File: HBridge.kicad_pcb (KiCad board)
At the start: 2 copper layers, 28 parts, among them Q1 DMG2301L, Q2 DMG3402L, Q3 DMG2301L, Q4 DMG3402L, U1 74LVC1GU04DRL, U10 LT1762, U2 74AHC1G08, U3 74AHC1G08, U4 74AHC1G08, U5 74AHC1G08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

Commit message: layout
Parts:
- moved C1 21.5 mm to (160.0, 97.0), turned to 90 degrees
- moved U1 20.0 mm to (162.5, 96.0), turned to 180 degrees
- moved STMInputEnable1 18.8 mm to (147.0, 77.0), turned to -90 degrees
- moved Q2 14.1 mm to (148.1, 89.0)
- moved U3 13.6 mm to (150.6, 94.5), turned to 180 degrees
- moved C5 13.6 mm to (149.7, 97.5), turned to 0 degrees
- moved C6 13.5 mm to (152.0, 80.5)
- moved Q3 13.5 mm to (155.0, 76.0)
- moved U4 13.5 mm to (155.0, 80.0)
- moved U8 13.5 mm to (155.9, 83.7)
- moved C8 12.9 mm to (154.0, 88.0)
- moved MotorLoad1 12.1 mm to (162.5, 79.8), turned to 180 degrees
- moved U6 11.6 mm to (154.0, 90.0)
- moved U2 11.3 mm to (162.5, 91.5), turned to 180 degrees
- moved Q1 7.28 mm to (158.0, 89.0), turned to 180 degrees
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
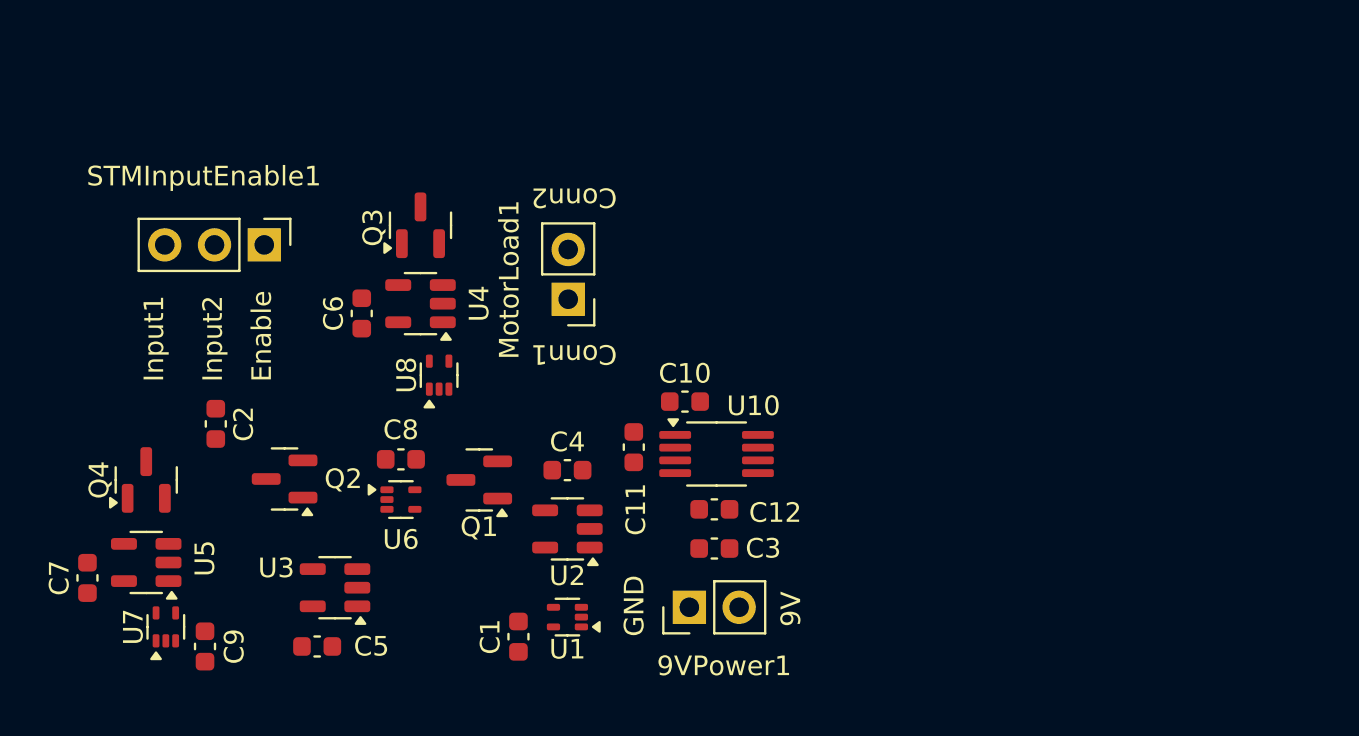
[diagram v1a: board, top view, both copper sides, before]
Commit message: fixed layout and added some routing
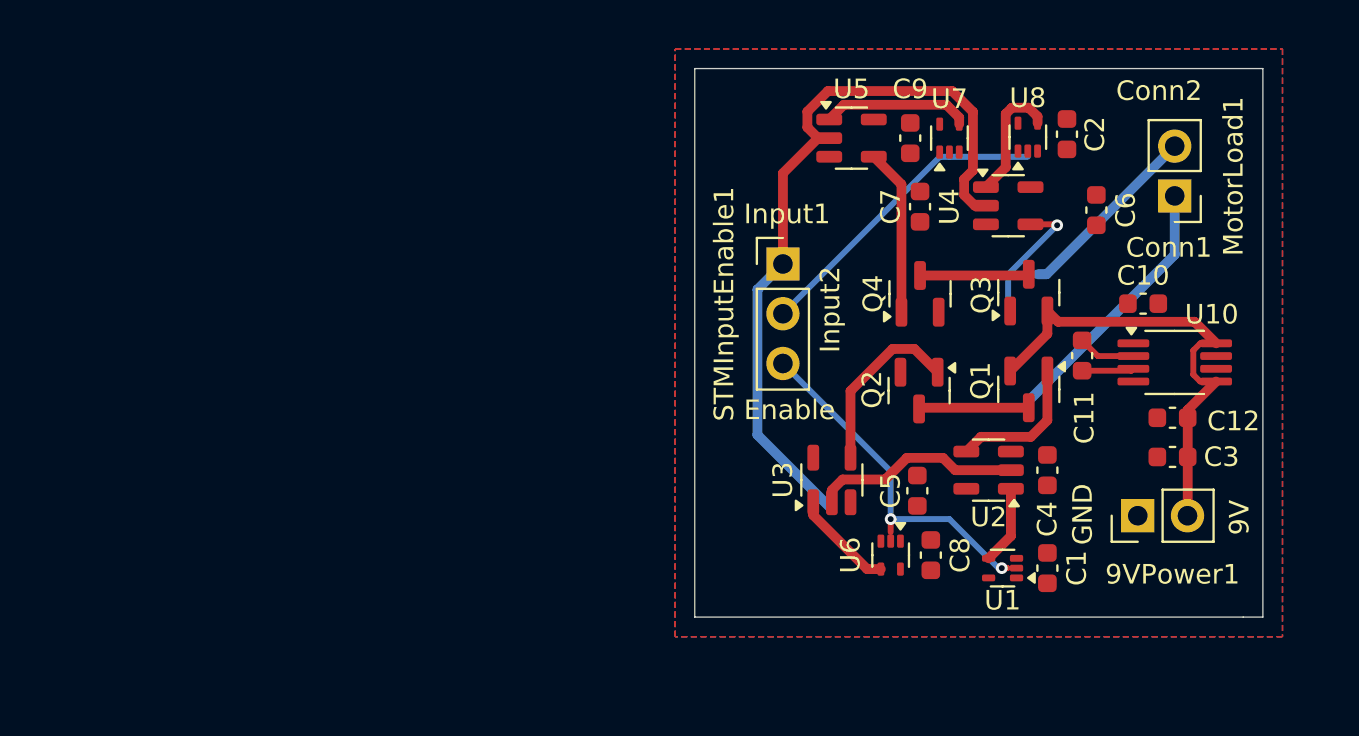
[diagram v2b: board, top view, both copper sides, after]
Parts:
- moved U7 47.1 mm to (182.0, 71.5)
- moved C7 46.5 mm to (180.5, 75.0)
- moved C2 45.9 mm to (188.0, 71.3)
- moved C9 44.4 mm to (180.0, 71.5)
- moved U5 42.0 mm to (177.0, 71.5), turned to 0 degrees
- moved Q4 40.6 mm to (180.5, 79.5)
- moved C6 37.9 mm to (189.5, 75.2)
- moved Q2 32.7 mm to (180.4, 84.4), turned to -90 degrees
- moved U8 32.4 mm to (186.0, 71.5)
- moved C5 31.7 mm to (180.4, 89.5), turned to 90 degrees
- moved MotorLoad1 31.4 mm to (193.5, 74.5)
- moved Q3 31.2 mm to (186.1, 79.4)
- moved U4 30.4 mm to (185.0, 75.0), turned to 0 degrees
- moved Q1 28.4 mm to (186.1, 84.4), turned to -90 degrees
- moved C8 27.5 mm to (181.1, 92.8), turned to 90 degrees
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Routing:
- net /Enable: track 0.00 -> 49.7 mm
- net +9V: track 0.00 -> 24.5 mm
- net /MotorConnect2: track 0.00 -> 19.2 mm
- net /Input1: track 0.00 -> 17.9 mm, vias 0 -> 2
- net /Input2: track 0.00 -> 15.8 mm
- net /MotorConnect1: track 0.00 -> 15.3 mm
- net Net-(Q2-G): track 0.00 -> 9.24 mm
- net Net-(Q4-G): track 0.00 -> 8.52 mm
- net Net-(U5-Pad1): track 0.00 -> 7.56 mm
- net Net-(Q1-G): track 0.00 -> 7.32 mm
- net Net-(Q3-G): track 0.00 -> 6.92 mm, vias 0 -> 1
- net Net-(U4-Pad1): track 0.00 -> 6.44 mm
- net Net-(U3-Pad1): track 0.00 -> 5.25 mm
- net Net-(U1-Pad4): track 0.00 -> 4.02 mm
- net Net-(U10-ADJ): track 0.00 -> 2.94 mm
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- added copper zone on B.Cu, net +3.3V
- added copper zone on F.Cu, net +3.3V
- added copper zone on B.Cu, net GND
- added copper zone on F.Cu, net GND
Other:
- board outline added: 29 x 28 mm

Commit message: Add files via upload
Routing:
- net +9V: track 24.5 -> 16.4 mm
- added copper zone on F.Cu, net +9V
- removed copper zone on F.Cu, net +3.3V
- removed copper zone on B.Cu, net GND
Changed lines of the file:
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@@
 	)
 	(setup
+		(stackup
+			(layer "F.SilkS"
+				(type "Top Silk Screen")
+			)
+			(layer "F.Paste"
+				(type "Top Solder Paste")
+			)
+			(layer "F.Mask"
+				(type "Top Solder Mask")
+				(thickness 0.01)
+			)
+			(layer "F.Cu"
+				(type "copper")
+				(thickness 0.035)
+			)
+			(layer "dielectric 1"
+				(type "core")
+				(thickness 1.51)
+				(material "FR4")
+				(epsilon_r 4.5)
+				(loss_tangent 0.02)
+			)
+			(layer "B.Cu"
+				(type "copper")
+				(thickness 0.035)
+			)
+			(layer "B.Mask"
+				(type "Bottom Solder Mask")
+				(thickness 0.01)
+			)
+			(layer "B.Paste"
+				(type "Bottom Solder Paste")
+			)
+			(layer "B.SilkS"
+				(type "Bottom Silk Screen")
+			)
+			(copper_finish "None")
+			(dielectric_constraints no)
+		)
 		(pad_to_mask_clearance 0)
 		(allow_soldermask_bridges_in_footprints no)
@@
 	)
 	(segment
-		(start 187 80.375)
-		(end 187 81.5375)
-		(width 0.5)
-		(layer "F.Cu")
-		(net 2)
-	)
-	(segment
-		(start 187 81.5375)
-		(end 185.1 83.4375)
-		(width 0.5)
+		(start 185.1 83.4375)
+		(end 185.1625 83.375)
+		(width 0.3)
 		(layer "F.Cu")
 		(net 2)
 	)
 	(segment
-		(start 194.1625 85.425)
-		(end 195.6125 83.975)
-		(width 0.5)
+		(start 185.1625 82.1625)
+		(end 185.325 82)
+		(width 0.3)
 		(layer "F.Cu")
 		(net 2)
 	)
 	(segment
-		(start 194.449 82.385418)
-		(end 194.449 83.623999)
+		(start 185.1 83.4375)
+		(end 185.1625 83.5)
 		(width 0.3)
 		(layer "F.Cu")
@@
 	)
 	(segment
-		(start 194.809418 82.025)
-		(end 194.449 82.385418)
+		(start 185.325 82)
+		(end 187 82)
 		(width 0.3)
 		(layer "F.Cu")
@@
 	)
 	(segment
-		(start 187.551 80.926)
-		(end 194.5135 80.926)
-		(width 0.5)
+		(start 185.1625 83.375)
+		(end 185.1625 82.1625)
+		(width 0.3)
 		(layer "F.Cu")
 		(net 2)
 	)
 	(segment
-		(start 194.449 83.623999)
-		(end 194.800001 83.975)
+		(start 186.875 80.5)
+		(end 187 80.375)
 		(width 0.3)
 		(layer "F.Cu")
@@
 	)
 	(segment
-		(start 194.1625 85.825)
-		(end 194.1625 85.425)
+		(start 187.551 80.926)
+		(end 194.5135 80.926)
 		(width 0.5)
 		(layer "F.Cu")
@@
 	)
 	(segment
-		(start 194.1625 87.825)
-		(end 194.1625 90.815)
-		(width 0.5)
+		(start 187 82)
+		(end 187 80.375)
+		(width 0.3)
 		(layer "F.Cu")
 		(net 2)
@@
 	(segment
 		(start 194.1625 85.825)
-		(end 194.1625 87.825)
+		(end 194.1625 85.425)
 		(width 0.5)
 		(layer "F.Cu")
@@
 	)
 	(zone
-		(net 3)
-		(net_name "+3.3V")
-		(layers "F.Cu" "B.Cu")
+		(net 1)
+		(net_name "GND")
+		(layer "F.Cu")
 		(hatch edge 0.5)
-		(priority 1)
 		(connect_pads
 			(clearance 0.5)
@@
 	)
 	(zone
-		(net 1)
-		(net_name "GND")
-		(layers "F.Cu" "B.Cu")
+		(net 2)
+		(net_name "+9V")
+		(layer "F.Cu")
 		(hatch edge 0.5)
+		(priority 2)
 		(connect_pads
 			(clearance 0.5)
@@
 		(polygon
 			(pts
-				(xy 168 67) (xy 199 67) (xy 199 97) (xy 168 97)
+				(xy 193.5 92) (xy 197 92) (xy 197 81) (xy 193.5 81)
+			)
+		)
+	)
+	(zone
+		(net 3)
+		(net_name "+3.3V")
+		(layer "B.Cu")
+		(hatch edge 0.5)
+		(priority 1)
+		(connect_pads
+			(clearance 0.5)
+		)
+		(min_thickness 0.25)
+		(filled_areas_thickness no)
+		(fill yes
+			(thermal_gap 0.5)
+			(thermal_bridge_width 0.5)
+		)
+		(polygon
+			(pts
+				(xy 174 95) (xy 174 69.5) (xy 194.5 69.5) (xy 194 95)
 			)
 		)

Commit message: finished routing
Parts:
- moved C5 5.89 mm to (174.5, 89.0)
- moved C7 4.94 mm to (176.0, 73.0)
- moved U5 3.99 mm to (179.0, 75.0)
- moved C8 2.23 mm to (180.5, 95.0), turned to 180 degrees
- moved U6 2.03 mm to (181.0, 92.5)
- moved U3 1.50 mm to (177.5, 89.0)
- moved C9 1.00 mm to (181.0, 71.5)
- moved U7 1.00 mm to (183.0, 71.5)
- moved Q1 0.33 mm to (186.0, 84.0)
- turned Q2 to 0 degrees
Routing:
- net +3.3V: track 0.00 -> 48.8 mm, vias 0 -> 8
- net /MotorConnect1: track 15.3 -> 25.8 mm, vias 0 -> 1
- net /Input2: track 15.8 -> 22.1 mm, vias 0 -> 1
- net /Enable: track 49.7 -> 44.1 mm, vias 0 -> 1
- net /Input1: track 17.9 -> 21.8 mm, vias 2 -> 1
- net Net-(Q4-G): track 8.52 -> 4.73 mm
- net /MotorConnect2: track 19.2 -> 22.7 mm, vias 0 -> 1
- net Net-(U5-Pad1): track 7.56 -> 10.7 mm
- net Net-(Q2-G): track 9.24 -> 6.98 mm
- net Net-(U3-Pad1): track 5.25 -> 6.64 mm
- net Net-(Q1-G): track 7.32 -> 8.43 mm, vias 0 -> 2
- net +9V: track 16.4 -> 17.4 mm
- net Net-(Q3-G): track 6.92 -> 6.35 mm, vias 1 -> 0

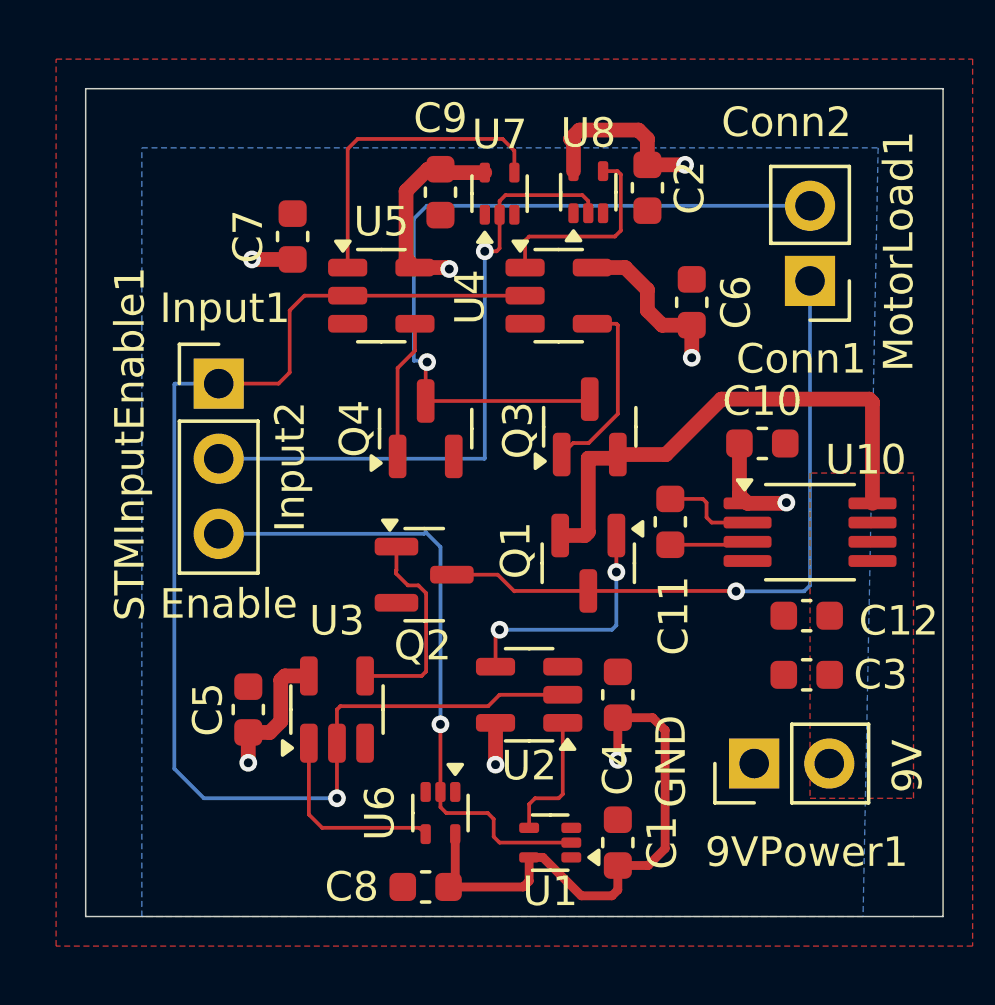
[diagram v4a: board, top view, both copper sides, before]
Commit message: layout and routing version 1
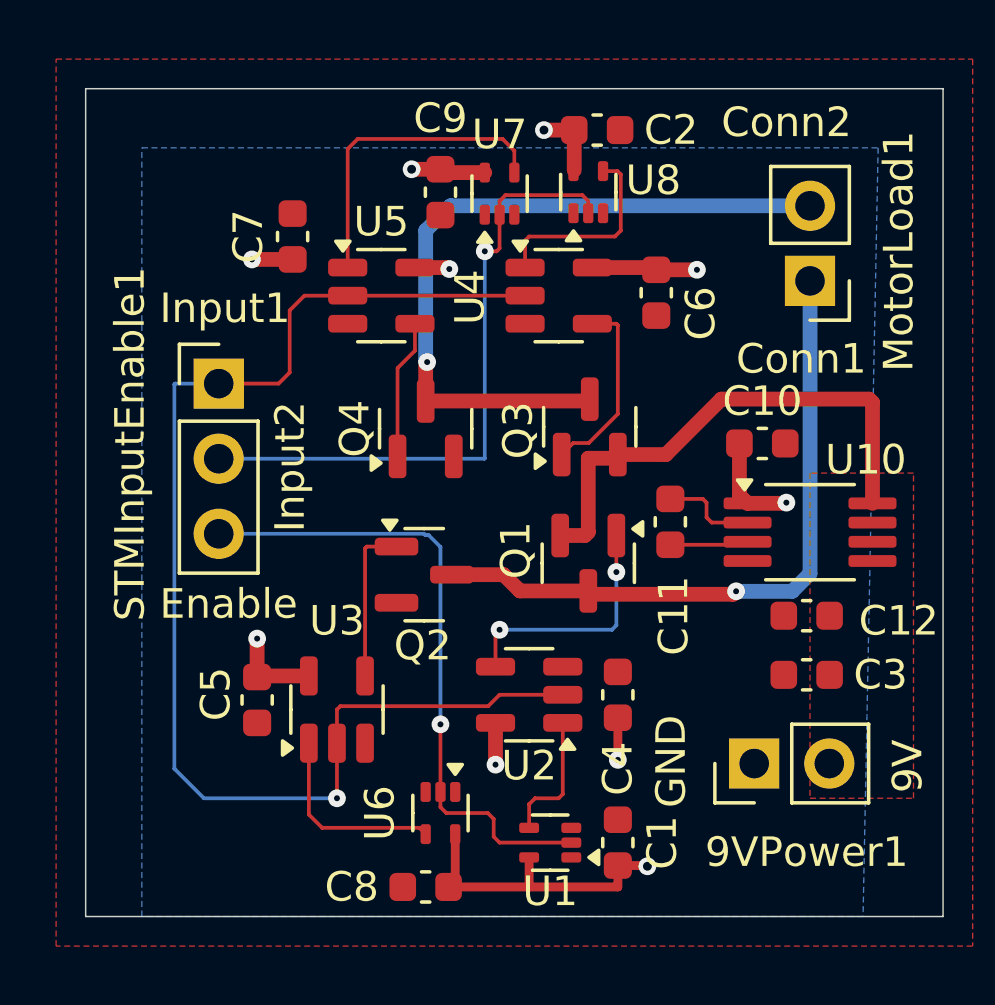
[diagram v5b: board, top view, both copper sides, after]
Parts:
- moved C2 2.59 mm to (186.3, 69.4), turned to 0 degrees
- moved C6 1.24 mm to (188.3, 74.9), turned to -90 degrees
- moved C5 0.44 mm to (174.8, 88.7), turned to -90 degrees
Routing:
- net +3.3V: track 48.8 -> 31.0 mm, vias 8 -> 10
- net Net-(Q2-G): track 6.98 -> 5.47 mm
- net /MotorConnect1: track 25.8 -> 24.8 mm

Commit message: layout and routing version 2
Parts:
- moved C7 5.95 mm to (181.6, 75.0), turned to -90 degrees
- moved C11 2.90 mm to (190.7, 84.8)
- moved C2 2.33 mm to (187.2, 71.5), turned to 90 degrees
- moved C10 2.29 mm to (193.3, 81.8)
- moved C5 1.94 mm to (176.0, 90.2)
- moved 9VPower1 1.90 mm to (192.9, 92.2)
- moved C9 1.90 mm to (182.1, 70.0), turned to 180 degrees
- moved U8 1.84 mm to (184.2, 71.9), turned to 0 degrees
- moved C1 1.84 mm to (186.6, 91.7)
- moved U3 1.80 mm to (179.2, 88.4), turned to 180 degrees
- moved C12 1.78 mm to (194.5, 87.2)
- moved C3 1.78 mm to (194.5, 89.2)
- moved U10 1.78 mm to (194.6, 84.4)
- moved U7 1.64 mm to (181.4, 71.9), turned to 180 degrees
- moved C8 1.17 mm to (181.6, 94.6)
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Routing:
- net +3.3V: track 31.0 -> 46.9 mm, vias 10 -> 6
- net /Enable: track 44.1 -> 35.6 mm
- net Net-(U4-Pad1): track 6.84 -> 1.82 mm
- net Net-(U5-Pad1): track 10.7 -> 6.01 mm
- net /MotorConnect1: track 24.8 -> 20.4 mm, vias 1 -> 0
- net +9V: track 17.4 -> 20.7 mm, vias 0 -> 2
- net Net-(Q1-G): track 8.43 -> 5.23 mm, vias 2 -> 0
- net Net-(U3-Pad1): track 6.64 -> 4.48 mm
- net Net-(Q3-G): track 6.35 -> 4.28 mm
- net /Input1: track 21.8 -> 19.7 mm
- net /Input2: track 22.1 -> 24.0 mm
- net Net-(Q2-G): track 5.47 -> 3.93 mm
- net Net-(U10-ADJ): track 3.24 -> 1.81 mm
- net /MotorConnect2: track 22.6 -> 23.5 mm
- net Net-(U1-Pad4): track 4.49 -> 5.00 mm
- added copper zone on F.Cu, net +3.3V
- added copper zone on B.Cu, net GND
- removed copper zone on B.Cu, net +3.3V
- removed copper zone on F.Cu, net GND
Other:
- board size 29 x 28 mm -> 30.4 x 28.7 mm
- board text added: "Motor1"
- board text added: "Motor2"
- board text removed: "Conn1"
- board text removed: "Conn2"

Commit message: Add files via upload
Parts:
- moved C4 4.00 mm to (183.0, 88.4)
- moved U2 2.30 mm to (186.0, 88.4)
- moved C1 0.91 mm to (186.7, 92.6)
- moved U6 0.73 mm to (181.8, 93.1), turned to 180 degrees
- moved C8 0.70 mm to (181.6, 95.3)
- moved C9 0.09 mm to (182.2, 70.0)
- moved U7 0.09 mm to (181.5, 71.9)
- moved U8 0.09 mm to (184.3, 71.9)
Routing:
- net +3.3V: track 46.9 -> 57.7 mm, vias 6 -> 4
- net +9V: track 20.7 -> 16.2 mm
- net /MotorConnect2: track 23.5 -> 20.9 mm
- net Net-(Q1-G): track 5.23 -> 2.81 mm
- net /Enable: track 35.6 -> 37.7 mm
- net Net-(U1-Pad4): track 5.00 -> 5.92 mm
- net Net-(U3-Pad1): track 4.48 -> 3.96 mm
- net Net-(U5-Pad1): track 6.01 -> 6.04 mm, vias 0 -> 2

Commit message: Add files via upload
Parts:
- moved C8 0.57 mm to (182.0, 94.9), turned to 0 degrees
- moved Q2 0.21 mm to (180.5, 83.7)
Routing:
- net GND: track 0.14 -> 28.4 mm, vias 0 -> 15
- net /Input2: track 24.0 -> 19.9 mm
- net /Input1: track 19.9 -> 17.5 mm
- net +3.3V: track 57.7 -> 55.6 mm
- net /Enable: track 37.7 -> 36.5 mm, vias 1 -> 0
- added copper zone on F.Cu, net GND
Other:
- board text added: "H-Bridge"
